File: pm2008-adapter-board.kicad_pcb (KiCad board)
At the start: 2 copper layers, 3 parts, among them J1 Conn_02x05_Top_Bottom, J2 Conn_01x04, J3 Conn_01x02

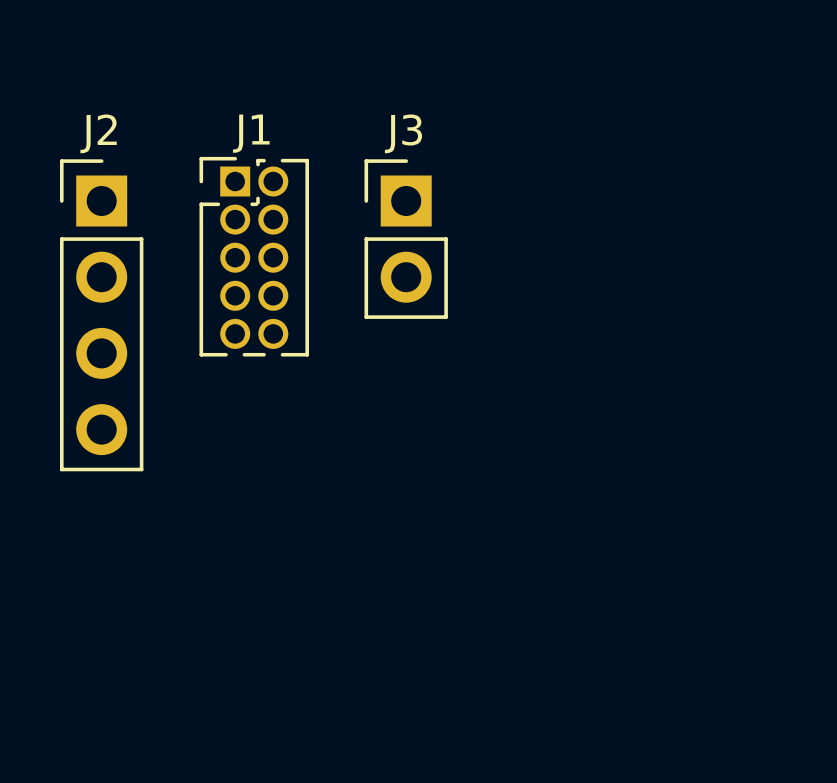
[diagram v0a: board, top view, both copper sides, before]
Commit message: feat: update artwork
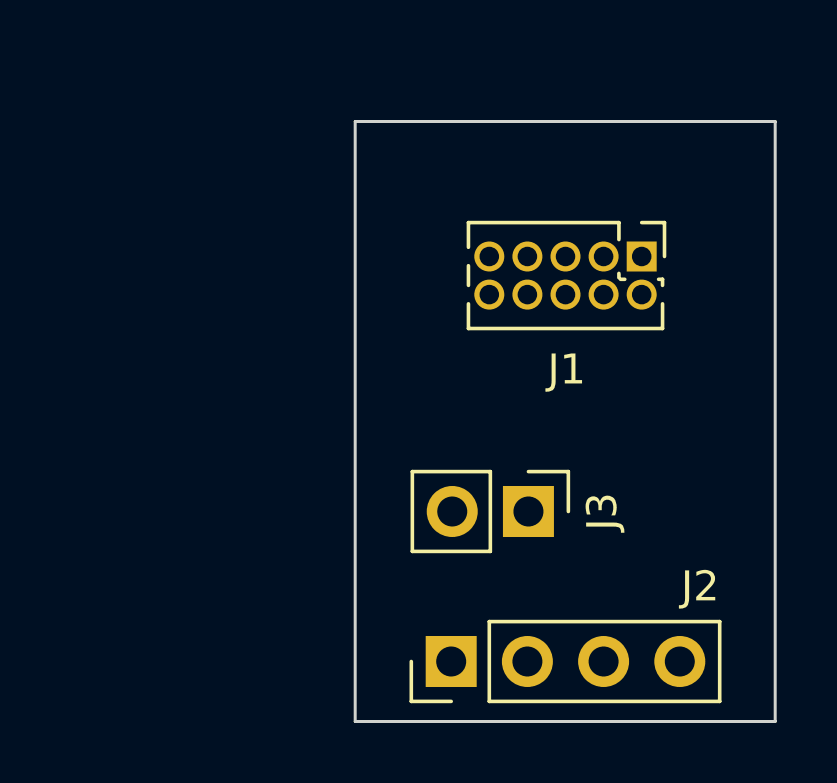
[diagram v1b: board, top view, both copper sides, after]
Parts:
- moved J2 19.3 mm to (143.2, 108.0), turned to 90 degrees
- moved J1 13.8 mm to (149.6, 94.5), turned to -90 degrees
- moved J3 11.1 mm to (145.8, 103.0), turned to -90 degrees
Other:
- board outline added: 14 x 20 mm
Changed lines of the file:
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@@
   )
   (paper "A4")
+  (title_block
+    (title "PM2008 Adapter Board")
+    (date "2022-10-28")
+    (rev "V01")
+    (company "neosarchizo")
+  )
   (layers
     (0 "F.Cu" signal)
@@
   (setup
     (pad_to_mask_clearance 0)
+    (grid_origin 140 90)
     (pcbplotparams
       (layerselection 0x00010fc_ffffffff)
@@
   (net 8 "unconnected-(J1-Pad10)")
   (footprint "Connector_PinHeader_1.27mm:PinHeader_2x05_P1.27mm_Vertical" (layer "F.Cu")
-    (at 136 92)
+    (at 149.55 94.5 -90)
     (descr "Through hole straight pin header, 2x05, 1.27mm pitch, double rows")
     (tags "Through hole pin header THT 2x05 1.27mm double row")
@@
     (property "Sheetname" "")
     (attr through_hole)
-    (fp_text reference "J1" (at 0.635 -1.695) (layer "F.SilkS")
-      (effects (font (size 1 1) (thickness 0.15)))
-    )
-    (fp_text value "Conn_02x05_Top_Bottom" (at 0.635 6.775) (layer "F.Fab")
-      (effects (font (size 1 1) (thickness 0.15)))
-    )
-    (fp_text user "${REFERENCE}" (at 0.635 2.54 90) (layer "F.Fab")
+    (fp_text reference "J1" (at 3.77 2.5) (layer "F.SilkS")
+      (effects (font (size 1 1) (thickness 0.15)))
+    )
+    (fp_text value "Conn_02x05_Top_Bottom" (at 0.635 6.775 90) (layer "F.Fab") hide
+      (effects (font (size 1 1) (thickness 0.15)))
+    )
+    (fp_text user "${REFERENCE}" (at 0.635 2.54) (layer "F.Fab")
       (effects (font (size 1 1) (thickness 0.15)))
     )
@@
     (fp_line (start 2.34 -0.635) (end 2.34 5.715) (layer "F.Fab") (width 0.1))
     (fp_line (start -0.2175 -0.635) (end 2.34 -0.635) (layer "F.Fab") (width 0.1))
-    (pad "1" thru_hole rect (at 0 0) (size 1 1) (drill 0.65) (layers *.Cu *.Mask)
+    (pad "1" thru_hole rect (at 0 0 270) (size 1 1) (drill 0.65) (layers *.Cu *.Mask)
       (net 1 "VDD") (pinfunction "Pin_1") (pintype "passive"))
-    (pad "2" thru_hole oval (at 1.27 0) (size 1 1) (drill 0.65) (layers *.Cu *.Mask)
+    (pad "2" thru_hole oval (at 1.27 0 270) (size 1 1) (drill 0.65) (layers *.Cu *.Mask)
       (net 1 "VDD") (pinfunction "Pin_2") (pintype "passive"))
-    (pad "3" thru_hole oval (at 0 1.27) (size 1 1) (drill 0.65) (layers *.Cu *.Mask)
+    (pad "3" thru_hole oval (at 0 1.27 270) (size 1 1) (drill 0.65) (layers *.Cu *.Mask)
       (net 2 "Earth") (pinfunction "Pin_3") (pintype "passive"))
-    (pad "4" thru_hole oval (at 1.27 1.27) (size 1 1) (drill 0.65) (layers *.Cu *.Mask)
+    (pad "4" thru_hole oval (at 1.27 1.27 270) (size 1 1) (drill 0.65) (layers *.Cu *.Mask)
       (net 2 "Earth") (pinfunction "Pin_4") (pintype "passive"))
-    (pad "5" thru_hole oval (at 0 2.54) (size 1 1) (drill 0.65) (layers *.Cu *.Mask)
+    (pad "5" thru_hole oval (at 0 2.54 270) (size 1 1) (drill 0.65) (layers *.Cu *.Mask)
       (net 3 "unconnected-(J1-Pad5)") (pinfunction "Pin_5") (pintype "passive+no_connect"))
-    (pad "6" thru_hole oval (at 1.27 2.54) (size 1 1) (drill 0.65) (layers *.Cu *.Mask)
+    (pad "6" thru_hole oval (at 1.27 2.54 270) (size 1 1) (drill 0.65) (layers *.Cu *.Mask)
       (net 4 "unconnected-(J1-Pad6)") (pinfunction "Pin_6") (pintype "passive+no_connect"))
-    (pad "7" thru_hole oval (at 0 3.81) (size 1 1) (drill 0.65) (layers *.Cu *.Mask)
+    (pad "7" thru_hole oval (at 0 3.81 270) (size 1 1) (drill 0.65) (layers *.Cu *.Mask)
       (net 5 "/RXD{slash}SDA") (pinfunction "Pin_7") (pintype "passive"))
-    (pad "8" thru_hole oval (at 1.27 3.81) (size 1 1) (drill 0.65) (layers *.Cu *.Mask)
+    (pad "8" thru_hole oval (at 1.27 3.81 270) (size 1 1) (drill 0.65) (layers *.Cu *.Mask)
       (net 6 "/CTL") (pinfunction "Pin_8") (pintype "passive"))
-    (pad "9" thru_hole oval (at 0 5.08) (size 1 1) (drill 0.65) (layers *.Cu *.Mask)
+    (pad "9" thru_hole oval (at 0 5.08 270) (size 1 1) (drill 0.65) (layers *.Cu *.Mask)
       (net 7 "/TXD{slash}SCL") (pinfunction "Pin_9") (pintype "passive"))
-    (pad "10" thru_hole oval (at 1.27 5.08) (size 1 1) (drill 0.65) (layers *.Cu *.Mask)
+    (pad "10" thru_hole oval (at 1.27 5.08 270) (size 1 1) (drill 0.65) (layers *.Cu *.Mask)
       (net 8 "unconnected-(J1-Pad10)") (pinfunction "Pin_10") (pintype "passive+no_connect"))
     (model "${KICAD6_3DMODEL_DIR}/Connector_PinHeader_1.27mm.3dshapes/PinHeader_2x05_P1.27mm_Vertical.wrl"
@@
   )
   (footprint "Connector_PinHeader_2.54mm:PinHeader_1x02_P2.54mm_Vertical" (layer "F.Cu")
-    (at 141.7 92.65)
+    (at 145.775 103 -90)
     (descr "Through hole straight pin header, 1x02, 2.54mm pitch, single row")
     (tags "Through hole pin header THT 1x02 2.54mm single row")
@@
     (property "Sheetname" "")
     (attr through_hole)
-    (fp_text reference "J3" (at 0 -2.33) (layer "F.SilkS")
-      (effects (font (size 1 1) (thickness 0.15)))
-    )
-    (fp_text value "Conn_01x02" (at 0 4.87) (layer "F.Fab")
-      (effects (font (size 1 1) (thickness 0.15)))
-    )
-    (fp_text user "${REFERENCE}" (at 0 1.27 90) (layer "F.Fab")
+    (fp_text reference "J3" (at 0 -2.46 90) (layer "F.SilkS")
+      (effects (font (size 1 1) (thickness 0.15)))
+    )
+    (fp_text value "Conn_01x02" (at 0 4.87 90) (layer "F.Fab") hide
+      (effects (font (size 1 1) (thickness 0.15)))
+    )
+    (fp_text user "${REFERENCE}" (at 0 1.27) (layer "F.Fab")
       (effects (font (size 1 1) (thickness 0.15)))
     )
@@
     (fp_line (start 1.27 -1.27) (end 1.27 3.81) (layer "F.Fab") (width 0.1))
     (fp_line (start -1.27 -0.635) (end -0.635 -1.27) (layer "F.Fab") (width 0.1))
-    (pad "1" thru_hole rect (at 0 0) (size 1.7 1.7) (drill 1) (layers *.Cu *.Mask)
+    (pad "1" thru_hole rect (at 0 0 270) (size 1.7 1.7) (drill 1) (layers *.Cu *.Mask)
       (net 6 "/CTL") (pinfunction "Pin_1") (pintype "passive"))
-    (pad "2" thru_hole oval (at 0 2.54) (size 1.7 1.7) (drill 1) (layers *.Cu *.Mask)
+    (pad "2" thru_hole oval (at 0 2.54 270) (size 1.7 1.7) (drill 1) (layers *.Cu *.Mask)
       (net 2 "Earth") (pinfunction "Pin_2") (pintype "passive"))
     (model "${KICAD6_3DMODEL_DIR}/Connector_PinHeader_2.54mm.3dshapes/PinHeader_1x02_P2.54mm_Vertical.wrl"
@@
   )
   (footprint "Connector_PinHeader_2.54mm:PinHeader_1x04_P2.54mm_Vertical" (layer "F.Cu")
-    (at 131.55 92.65)
+    (at 143.2 108 90)
     (descr "Through hole straight pin header, 1x04, 2.54mm pitch, single row")
     (tags "Through hole pin header THT 1x04 2.54mm single row")
@@
     (property "Sheetname" "")
     (attr through_hole)
-    (fp_text reference "J2" (at 0 -2.33) (layer "F.SilkS")
-      (effects (font (size 1 1) (thickness 0.15)))
-    )
-    (fp_text value "Conn_01x04" (at 0 9.95) (layer "F.Fab")
-      (effects (font (size 1 1) (thickness 0.15)))
-    )
-    (fp_text user "${REFERENCE}" (at 0 3.81 90) (layer "F.Fab")
+    (fp_text reference "J2" (at 2.5 8.3 180) (layer "F.SilkS")
+      (effects (font (size 1 1) (thickness 0.15)))
+    )
+    (fp_text value "Conn_01x04" (at 0 9.95 90) (layer "F.Fab") hide
+      (effects (font (size 1 1) (thickness 0.15)))
+    )
+    (fp_text user "${REFERENCE}" (at 0 3.81) (layer "F.Fab")
       (effects (font (size 1 1) (thickness 0.15)))
     )
@@
     (fp_line (start 1.27 8.89) (end -1.27 8.89) (layer "F.Fab") (width 0.1))
     (fp_line (start -0.635 -1.27) (end 1.27 -1.27) (layer "F.Fab") (width 0.1))
-    (pad "1" thru_hole rect (at 0 0) (size 1.7 1.7) (drill 1) (layers *.Cu *.Mask)
+    (pad "1" thru_hole rect (at 0 0 90) (size 1.7 1.7) (drill 1) (layers *.Cu *.Mask)
       (net 1 "VDD") (pinfunction "Pin_1") (pintype "passive"))
-    (pad "2" thru_hole oval (at 0 2.54) (size 1.7 1.7) (drill 1) (layers *.Cu *.Mask)
+    (pad "2" thru_hole oval (at 0 2.54 90) (size 1.7 1.7) (drill 1) (layers *.Cu *.Mask)
       (net 2 "Earth") (pinfunction "Pin_2") (pintype "passive"))
-    (pad "3" thru_hole oval (at 0 5.08) (size 1.7 1.7) (drill 1) (layers *.Cu *.Mask)
+    (pad "3" thru_hole oval (at 0 5.08 90) (size 1.7 1.7) (drill 1) (layers *.Cu *.Mask)
       (net 5 "/RXD{slash}SDA") (pinfunction "Pin_3") (pintype "passive"))
-    (pad "4" thru_hole oval (at 0 7.62) (size 1.7 1.7) (drill 1) (layers *.Cu *.Mask)
+    (pad "4" thru_hole oval (at 0 7.62 90) (size 1.7 1.7) (drill 1) (layers *.Cu *.Mask)
       (net 7 "/TXD{slash}SCL") (pinfunction "Pin_4") (pintype "passive"))
     (model "${KICAD6_3DMODEL_DIR}/Connector_PinHeader_2.54mm.3dshapes/PinHeader_1x04_P2.54mm_Vertical.wrl"
@@
     )
   )
+  (gr_line (start 140 110) (end 154 110) (layer "Edge.Cuts") (width 0.1))
+  (gr_line (start 140 110) (end 140 90) (layer "Edge.Cuts") (width 0.1))
+  (gr_line (start 140 90) (end 154 90) (layer "Edge.Cuts") (width 0.1))
+  (gr_line (start 154 90) (end 154 110) (layer "Edge.Cuts") (width 0.1))
 )

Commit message: feat: update artwork
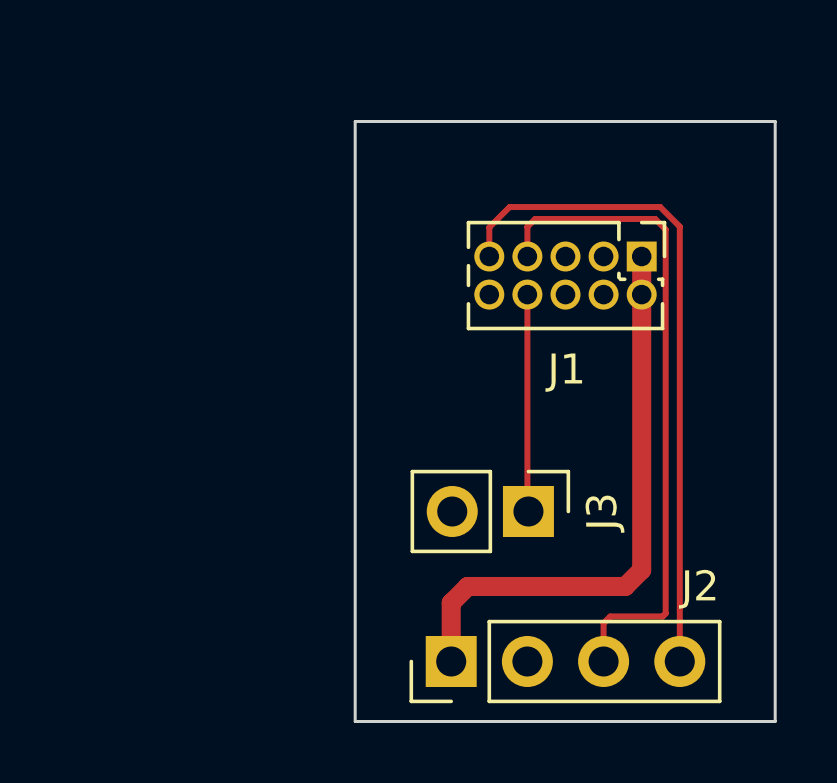
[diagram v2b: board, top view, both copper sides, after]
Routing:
- net /TXD/SCL: track 0.00 -> 22.4 mm
- net /RXD/SDA: track 0.00 -> 22.1 mm
- net VDD: track 0.00 -> 19.2 mm
- net /CTL: track 0.00 -> 7.24 mm
- added copper zone on B.Cu, net Earth
- added copper zone on F.Cu, net Earth
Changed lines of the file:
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@@
   )
   (setup
+    (stackup
+      (layer "F.SilkS" (type "Top Silk Screen"))
+      (layer "F.Paste" (type "Top Solder Paste"))
+      (layer "F.Mask" (type "Top Solder Mask") (thickness 0.01))
+      (layer "F.Cu" (type "copper") (thickness 0.035))
+      (layer "dielectric 1" (type "core") (thickness 1.51) (material "FR4") (epsilon_r 4.5) (loss_tangent 0.02))
+      (layer "B.Cu" (type "copper") (thickness 0.035))
+      (layer "B.Mask" (type "Bottom Solder Mask") (thickness 0.01))
+      (layer "B.Paste" (type "Bottom Solder Paste"))
+      (layer "B.SilkS" (type "Bottom Silk Screen"))
+      (copper_finish "None")
+      (dielectric_constraints no)
+    )
     (pad_to_mask_clearance 0)
     (grid_origin 140 90)
@@
   (gr_line (start 140 90) (end 154 90) (layer "Edge.Cuts") (width 0.1))
   (gr_line (start 154 90) (end 154 110) (layer "Edge.Cuts") (width 0.1))
+  (segment (start 149 105.5) (end 149.55 104.95) (width 0.635) (layer "F.Cu") (net 1))
+  (segment (start 149.55 104.95) (end 149.55 95.77) (width 0.635) (layer "F.Cu") (net 1))
+  (segment (start 143.2 108) (end 143.2 106.05) (width 0.635) (layer "F.Cu") (net 1))
+  (segment (start 149.55 95.77) (end 149.55 94.5) (width 0.635) (layer "F.Cu") (net 1))
+  (segment (start 143.75 105.5) (end 149 105.5) (width 0.635) (layer "F.Cu") (net 1))
+  (segment (start 143.2 106.05) (end 143.75 105.5) (width 0.635) (layer "F.Cu") (net 1))
+  (segment (start 145.74 93.51) (end 146 93.25) (width 0.2) (layer "F.Cu") (net 5))
+  (segment (start 150.25 106.5) (end 148.5 106.5) (width 0.2) (layer "F.Cu") (net 5))
+  (segment (start 148.5 106.5) (end 148.28 106.72) (width 0.2) (layer "F.Cu") (net 5))
+  (segment (start 146 93.25) (end 150 93.25) (width 0.2) (layer "F.Cu") (net 5))
+  (segment (start 145.74 94.5) (end 145.74 93.51) (width 0.2) (layer "F.Cu") (net 5))
+  (segment (start 150.349511 93.599511) (end 150.349511 106.400489) (width 0.2) (layer "F.Cu") (net 5))
+  (segment (start 150 93.25) (end 150.349511 93.599511) (width 0.2) (layer "F.Cu") (net 5))
+  (segment (start 150.349511 106.400489) (end 150.25 106.5) (width 0.2) (layer "F.Cu") (net 5))
+  (segment (start 148.28 106.72) (end 148.28 108) (width 0.2) (layer "F.Cu") (net 5))
+  (segment (start 145.74 95.77) (end 145.74 102.965) (width 0.2) (layer "F.Cu") (net 6))
+  (segment (start 145.74 102.965) (end 145.775 103) (width 0.2) (layer "F.Cu") (net 6))
+  (segment (start 144.47 93.53) (end 145.149519 92.850481) (width 0.2) (layer "F.Cu") (net 7))
+  (segment (start 150.165487 92.850481) (end 150.82 93.504994) (width 0.2) (layer "F.Cu") (net 7))
+  (segment (start 144.47 94.5) (end 144.47 93.53) (width 0.2) (layer "F.Cu") (net 7))
+  (segment (start 145.149519 92.850481) (end 150.165487 92.850481) (width 0.2) (layer "F.Cu") (net 7))
+  (segment (start 150.82 93.504994) (end 150.82 108) (width 0.2) (layer "F.Cu") (net 7))
+  (zone (net 2) (net_name "Earth") (layers F&B.Cu) (hatch edge 0.508)
+    (connect_pads (clearance 0.508))
+    (min_thickness 0.254) (filled_areas_thickness no)
+    (fill yes (thermal_gap 0.508) (thermal_bridge_width 0.508))
+    (polygon
+      (pts
+        (xy 154 110)
+        (xy 140 110)
+        (xy 140 90)
+        (xy 154 90)
+      )
+    )
+  )
 )

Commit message: feat: update component
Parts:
- J1: footprint Connector_PinHeader_1.27mm:PinHeader_2x05_P1.27mm_Vertical -> Connector_PinSocket_1.27mm:PinSocket_2x05_P1.27mm_Vertical
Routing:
- net /TXD/SCL: track 22.4 -> 44.5 mm
- net /RXD/SDA: track 22.1 -> 0.00 mm
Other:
- board text added: "GND"
- board text added: "RXD SDA"
- board text added: "TXD SCL"
- board text added: "VDD"
